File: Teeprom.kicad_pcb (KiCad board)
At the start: 2 copper layers, 16 x 38 mm, 4 parts, among them J1 Tandy_100_102_200_option_rom, U1 28C256

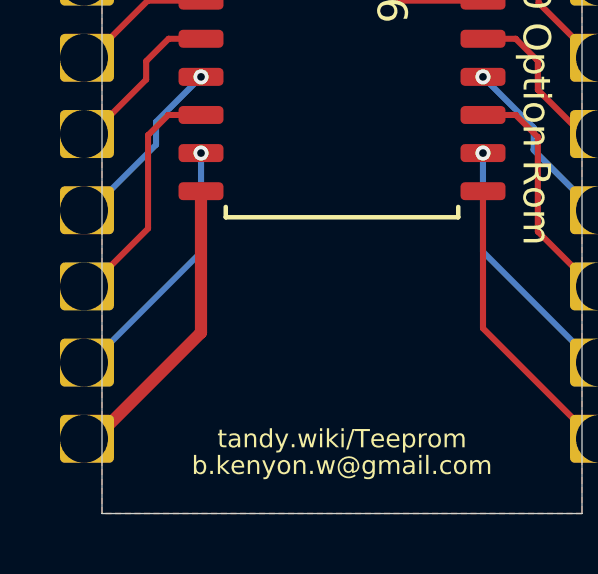
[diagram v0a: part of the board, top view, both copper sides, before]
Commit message: gitignore, remove explicit gnd trace
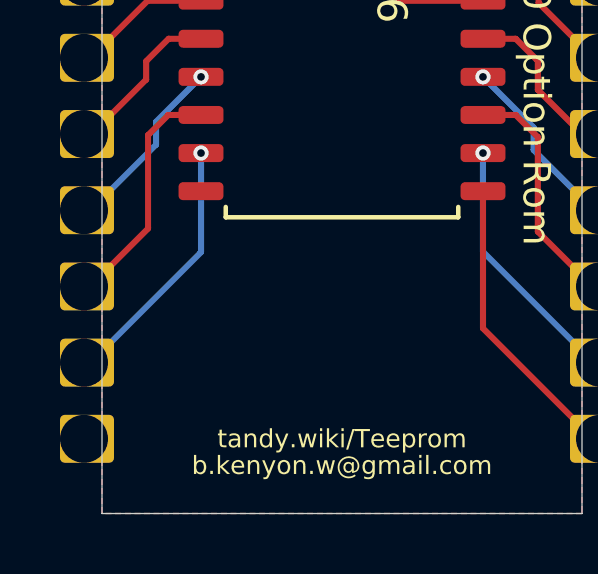
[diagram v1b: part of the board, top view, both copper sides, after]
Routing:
- net /VSS: track 9.99 -> 0.27 mm

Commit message: minor
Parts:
- R1: footprint Resistors_SMD:R_0805 -> 000_LOCAL:R_0805_2012Metric
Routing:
- net /VSS: track 0.27 -> 0.00 mm, vias 4 -> 1
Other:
- outline, holes or cut-outs redrawn

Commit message: cosmetics
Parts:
- removed carrier?: pcb2molex8878_chamfer, 000_LOCAL:pcb2molex8878_chamfer
- J1: footprint 000_LOCAL:pcb2molex8878 -> 000_LOCAL:Molex78805_PCB
- R1: footprint 000_LOCAL:R_0805_2012Metric -> 000_LOCAL:R_0805
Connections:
- net /VCC renamed VCC
- net /VSS renamed GND
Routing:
- net GND: track 0.00 -> 9.95 mm, vias 1 -> 0
- net /A8: track 15.9 -> 8.89 mm
- net /A10: track 21.6 -> 27.5 mm, vias 1 -> 0
- net /~CE: track 25.9 -> 21.7 mm
- net /A13: track 6.09 -> 9.34 mm, vias 1 -> 0
- net /A11: track 8.01 -> 9.78 mm
- net VCC: track 19.6 -> 18.7 mm
- net /A14: track 17.4 -> 16.6 mm
- net /D7: track 5.69 -> 5.12 mm
- net /~WE: track 4.73 -> 4.17 mm
- net /A6: track 6.08 -> 6.54 mm, vias 1 -> 0
- net /D4: track 8.63 -> 8.94 mm, vias 1 -> 0
- net /D6: track 6.09 -> 6.40 mm, vias 1 -> 0
- net /D0: track 6.10 -> 6.40 mm, vias 1 -> 0
- net /D2: track 8.64 -> 8.94 mm, vias 1 -> 0
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- removed copper zone on B.Cu, net GND
- removed copper zone on F.Cu, net GND
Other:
- board size 16 x 38 mm -> 16.5 x 38 mm
- net class Default: clearance 0.2032 -> 0.2; trace_width 0.2032 -> 0.2; via_dia 0.508 -> 0.5; via_drill 0.254 -> 0.3
- rule trace_clearance: 0.2032 -> 0.2
- rule trace_min: 0.1524 -> 0.2
- rule via_min_drill: 0.254 -> 0.3
- rule via_min_size: 0.508 -> 0.5
- board text added: "Use with carrier: http://shpws.me/RqW3"
- board text added: "github.com/bkw777/Teeprom"
- board text removed: "Use with thingiverse.com/thing:3821586"
- board text removed: "b.kenyon.w@gmail.com"
- board text removed: "tandy.wiki/Teeprom"

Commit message: update to v004 board outline and carrier
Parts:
- J1: footprint 000_LOCAL:Molex78805_PCB -> 000_LOCAL:Molex78802_PCB_28
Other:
- board size 16.5 x 38 mm -> 16.6 x 38 mm
- board text added: "v004"

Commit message: silkscreens
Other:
- board text added: "28C256"
- board text added: "Carrier: Molex78802_PCB_28 v004"
- board text added: "tandy.wiki/Teeprom v004"
- board text removed: "Use with carrier: http://shpws.me/RqW3"
- board text removed: "github.com/bkw777/Teeprom"
- board text removed: "v004"

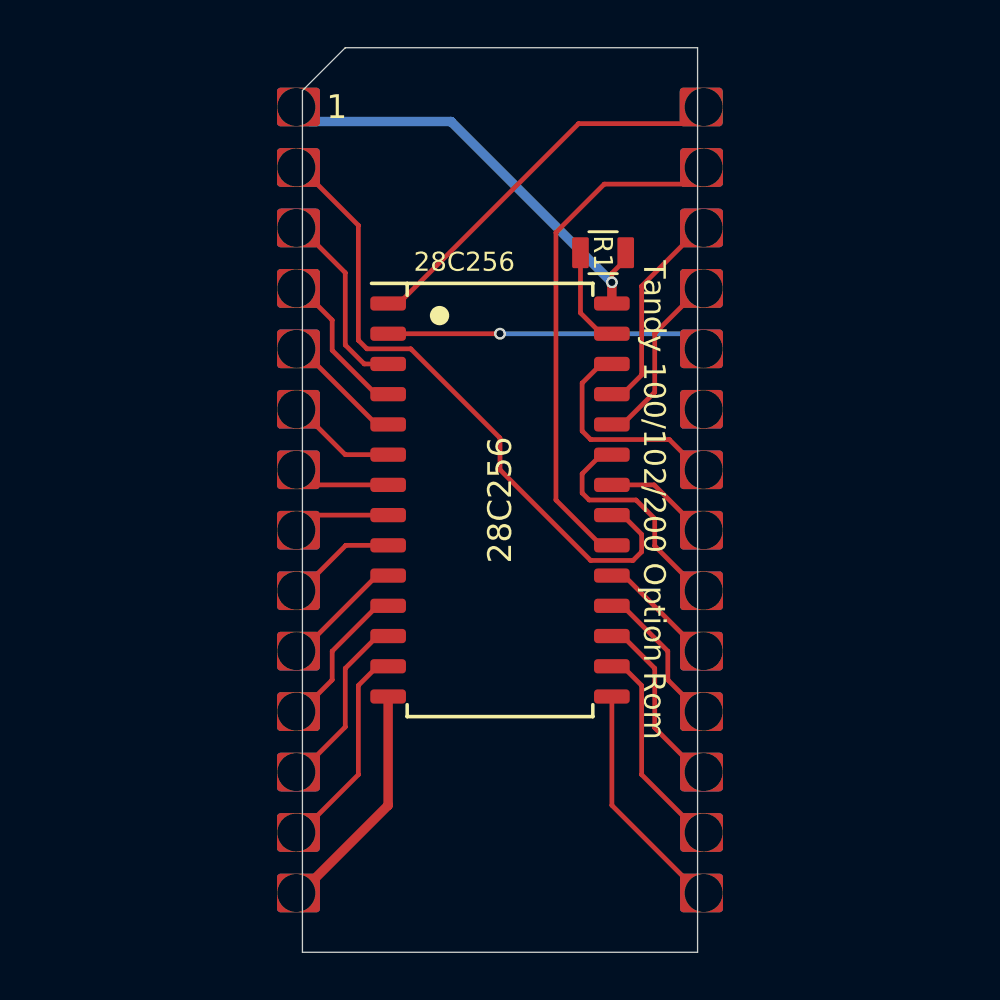
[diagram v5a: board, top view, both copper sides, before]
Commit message: kicad 6, flashopt100 programming socket
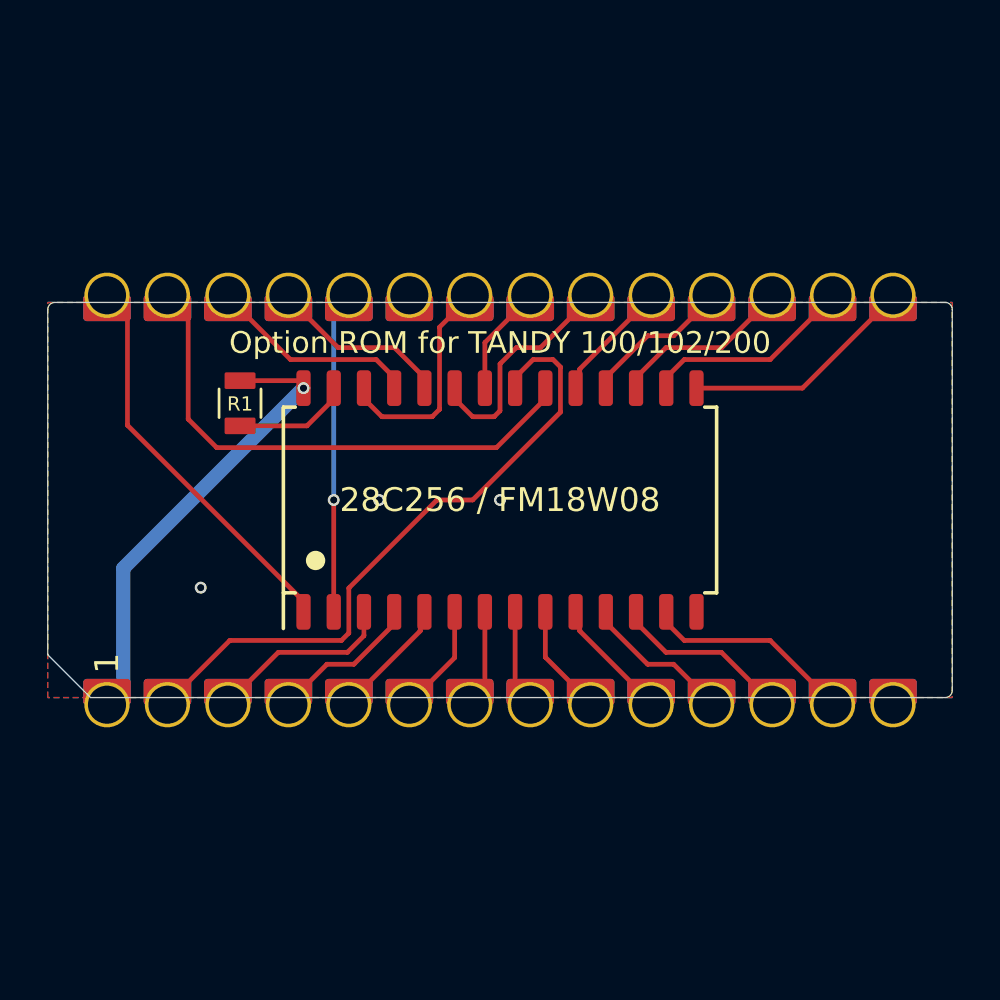
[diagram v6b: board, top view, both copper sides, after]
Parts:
- U1: value 28C256 -> 28C256 / FM18W08
- moved R1 16.5 mm to (136.3, 95.1), turned to 90 degrees
- turned J1 to 90 degrees
- turned U1 to 90 degrees
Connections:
- net /~CE renamed /~{CE}
- net /~OE renamed /~{OE}
- net /~WE renamed /~{WE}
- J1 pad 23: (no net) -> unconnected-(J1-Pad23)
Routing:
- net GND: track 9.95 -> 0.00 mm, vias 0 -> 3
- net VCC: track 18.7 -> 19.7 mm
- net /~{WE}: track 4.17 -> 4.86 mm
- net /~{CE}: track 21.7 -> 22.4 mm
- added copper zone on B.Cu, net GND
- added copper zone on F.Cu, net GND
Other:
- board size 16.6 x 38 mm -> 38 x 16.6 mm
- net class Default removed
- board text added: "${COMMENT2} ${REVISION}"
- board text added: "${COMMENT3}"
- board text added: "R1: ${00000000-0000-0000-0000-00005d22c129:VALUE} ${COMMENT4}"
- board text removed: "28C256"
- board text removed: "Carrier: Molex78802_PCB_28 v004"
- board text removed: "R1: 47k"
- board text removed: "Tandy 100/102/200 Option Rom"
- board text removed: "tandy.wiki/Teeprom v004"
